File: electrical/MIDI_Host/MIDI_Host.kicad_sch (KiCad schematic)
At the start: 45 parts, among them CN1 USB-CON-AF-LCP-Offset, J1 MC-107DM, J2 (NF), SW1 ST-0-102-C03-N003-RS, SW2 TC-1109DE-C-G, U11 BL1551B, U12 BL1551B, U14 SESRV05-4, U15 SESRV05-4, U16 BL1551B, U17 74HC165, U4 ESP32-S3-WROOM-1U, U8 BL1551B

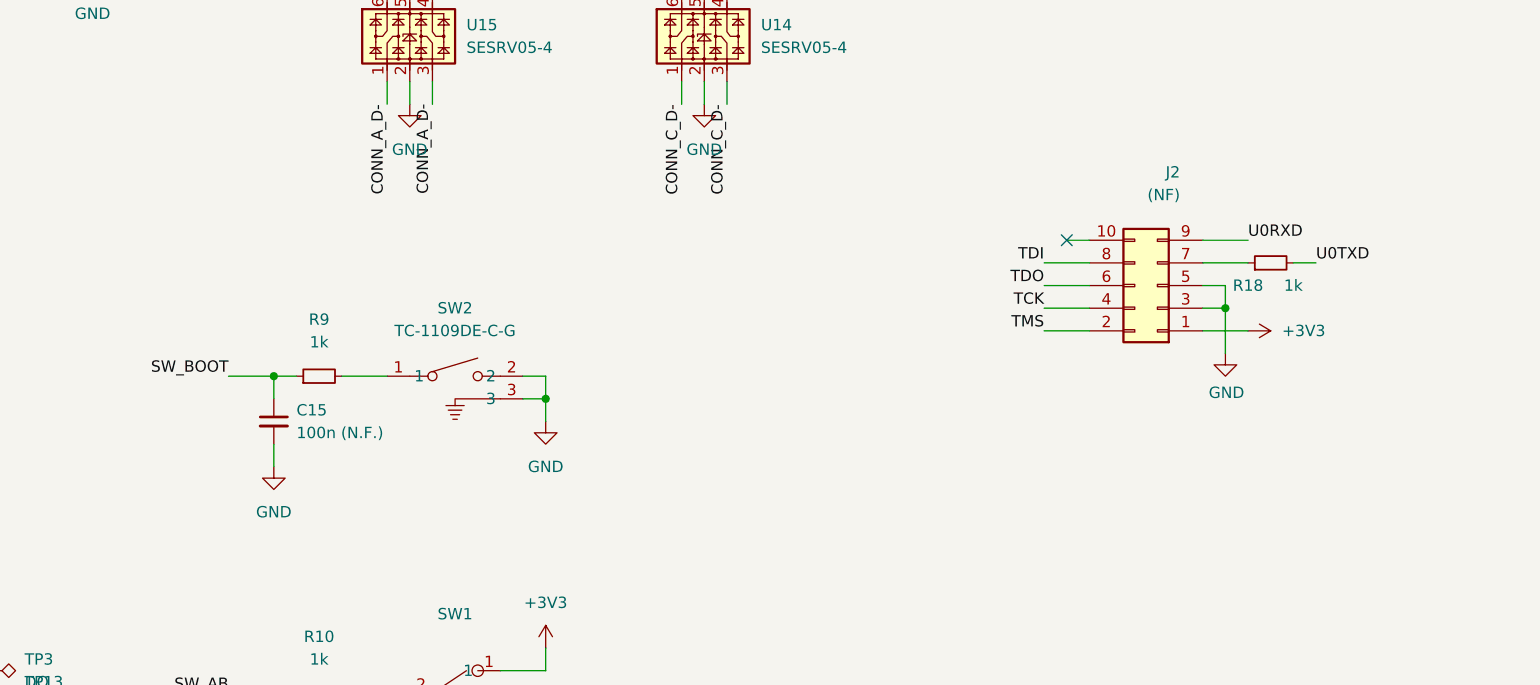
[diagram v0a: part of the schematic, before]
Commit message: SUKU sync + fw connect status led function added
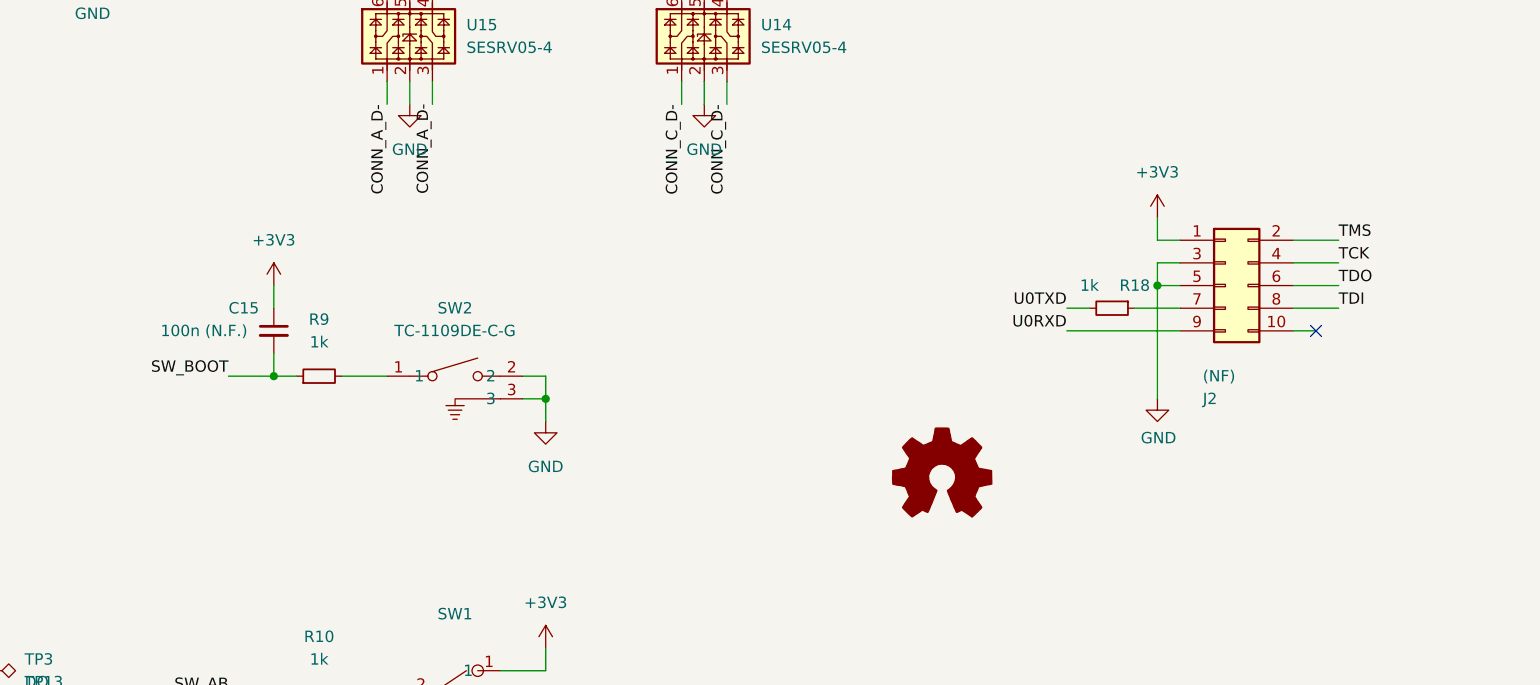
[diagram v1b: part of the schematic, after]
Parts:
- added LOGO1: OSHWA, suku_basics:OSHWA_KNOT, symbol suku_basics:OSHWA
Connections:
- net +3V3: now also C15.1
- net GND: no longer C15.2
- net SW_BOOT: now also C15.2; no longer C15.1
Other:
- moved on the sheet: C15, J2, R18

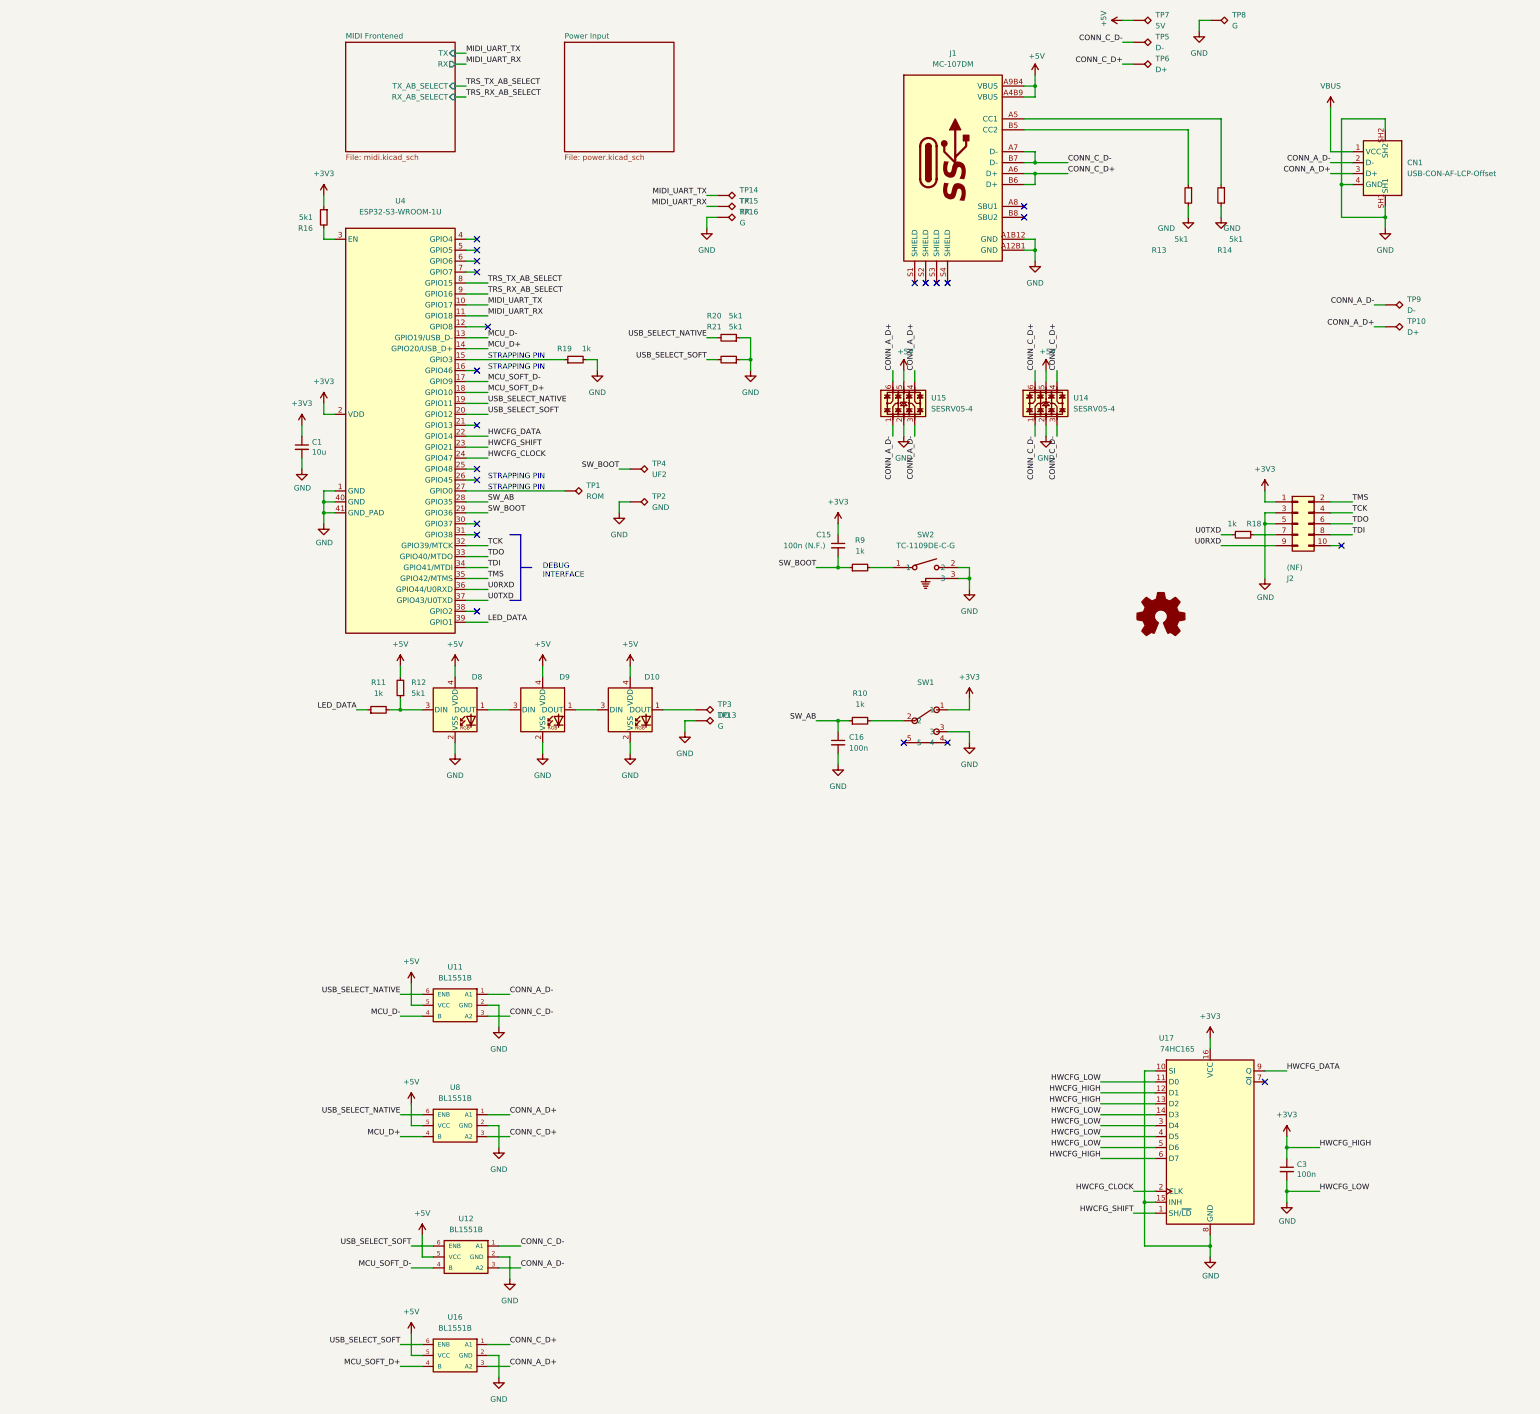
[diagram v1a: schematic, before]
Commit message: SUKU connectors moved back, gerber testpoint names fixed
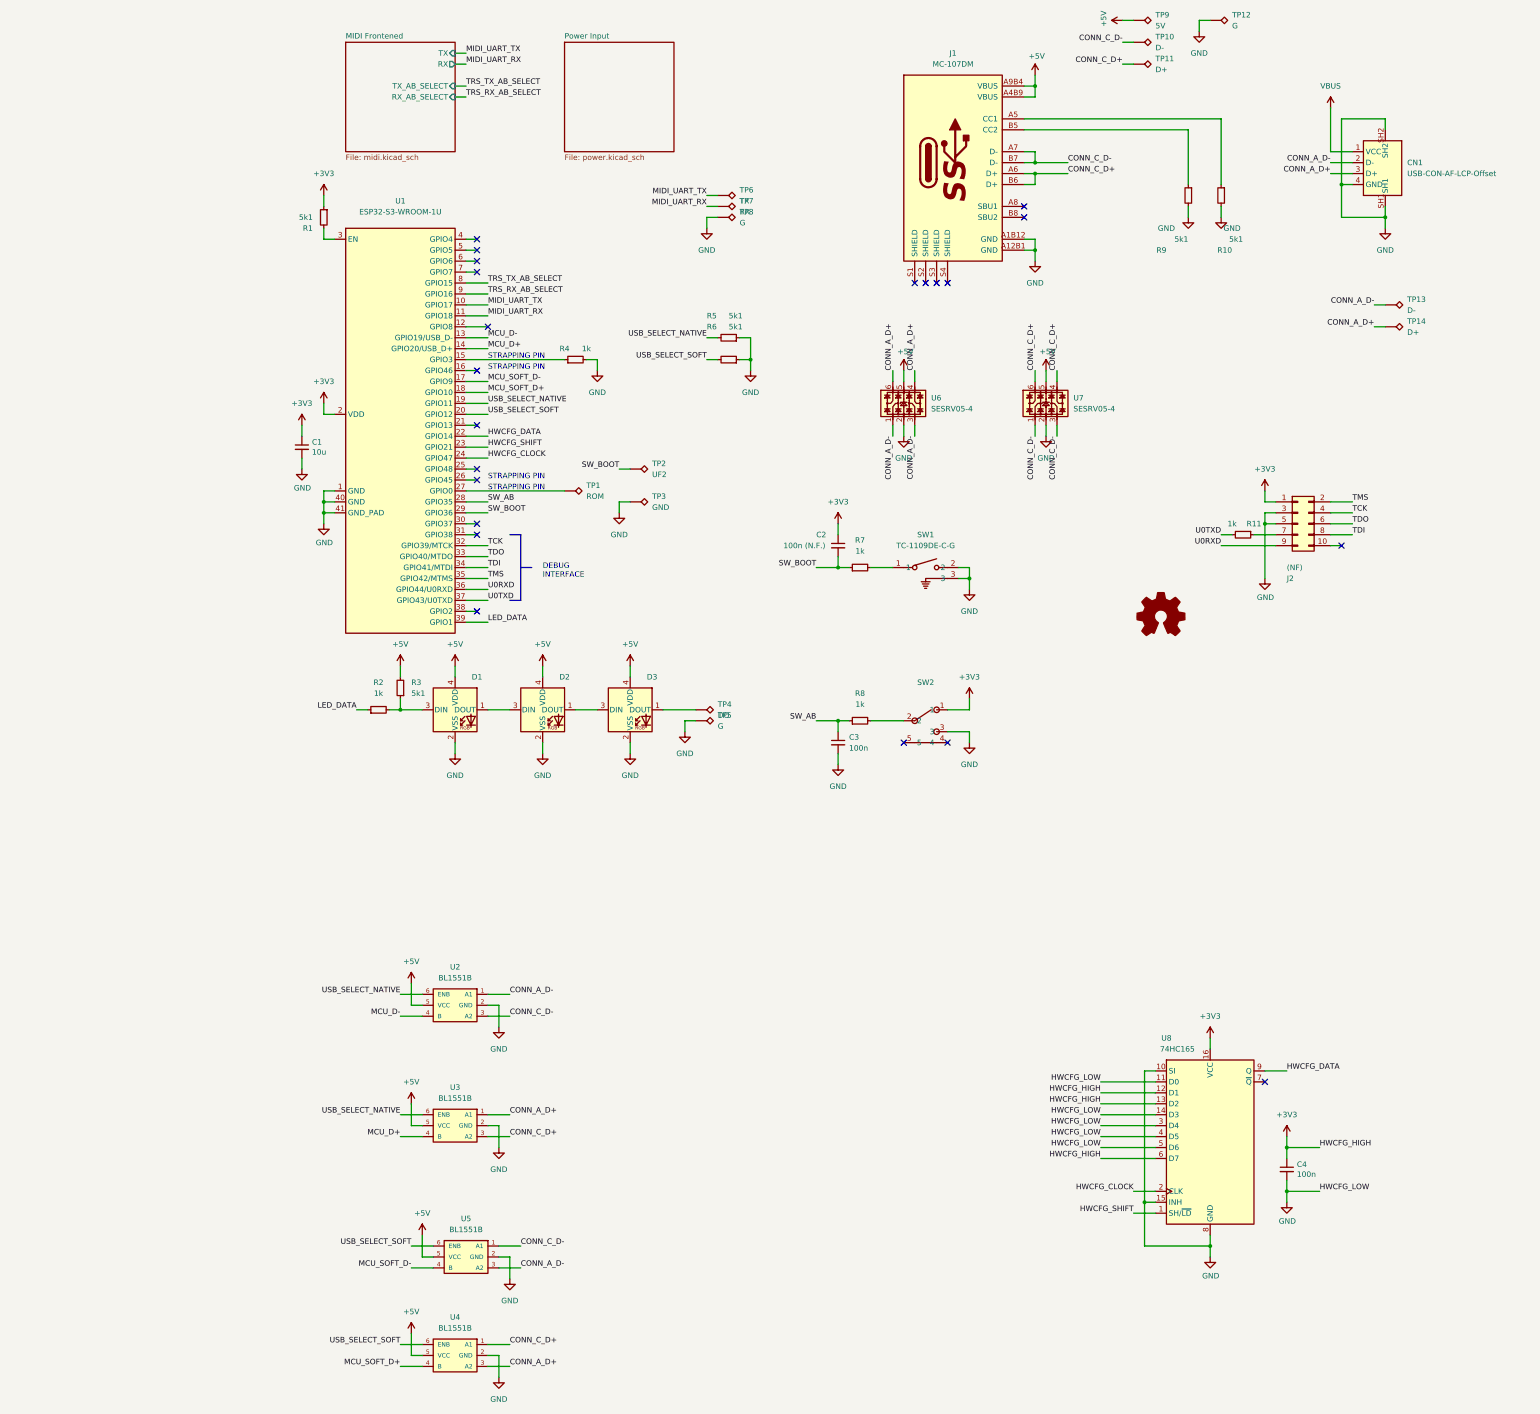
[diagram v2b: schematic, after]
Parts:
- renumbered C15 to C2, C16 to C3, C3 to C4, D8 to D1, D9 to D2, D10 to D3, R16 to R1, R14 to R10, R18 to R11, R11 to R2, R12 to R3, R19 to R4, R20 to R5, R21 to R6, R9 to R7, R10 to R8, R13 to R9, SW2 to SW1, SW1 to SW2, TP5 to TP10, TP6 to TP11, TP8 to TP12, TP9 to TP13, TP10 to TP14, TP4 to TP2, TP2 to TP3, TP3 to TP4, TP13 to TP5, TP14 to TP6, TP15 to TP7, TP16 to TP8, TP7 to TP9, U4 to U1, U11 to U2, U8 to U3, U16 to U4, U12 to U5, U15 to U6, U14 to U7, U17 to U8

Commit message: SUKU v3 laout finished, decoupling and esd protection improved
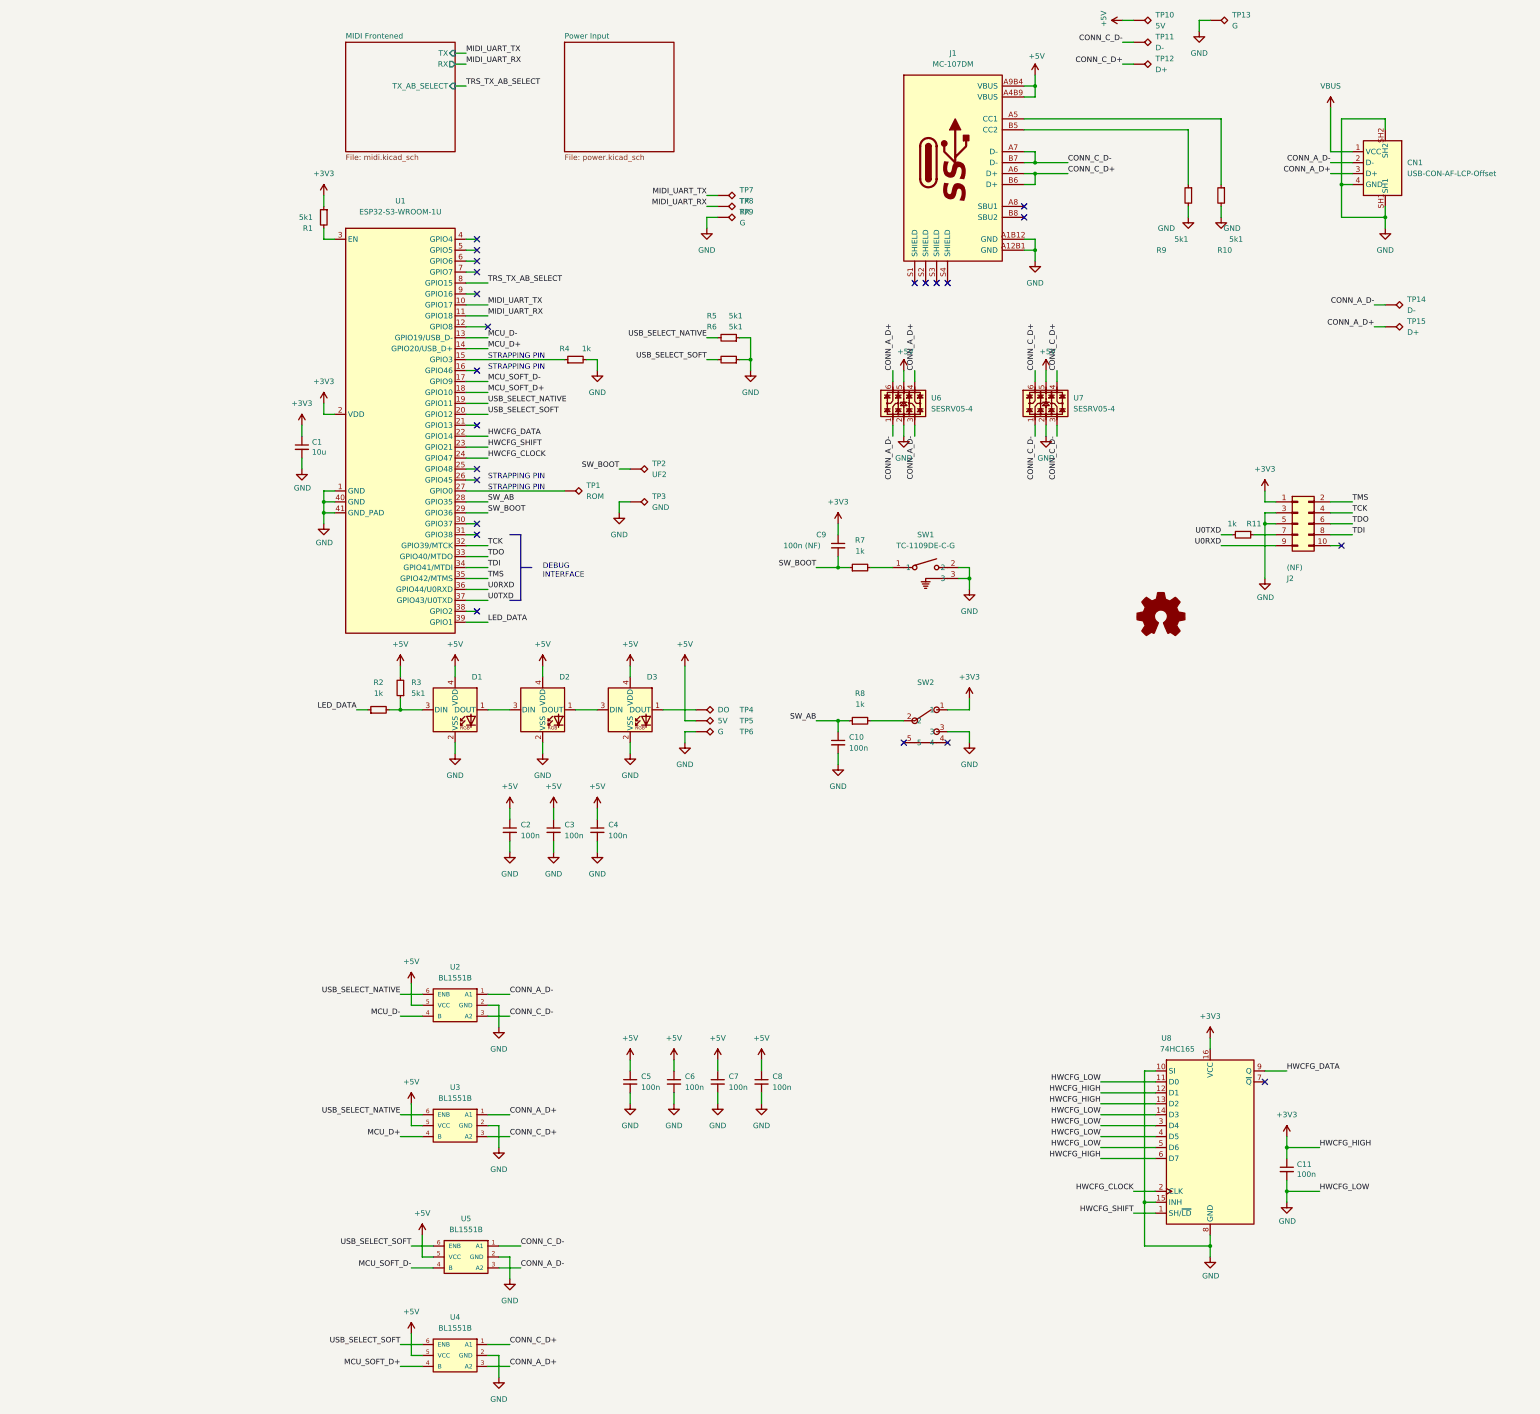
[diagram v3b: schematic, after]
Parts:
- added C2, C3, C4, C5, C6, C7, C8: 100n, suku_basics:CAP_0402, symbol suku_basics:CAP
- added TP5: 5V, TestPoint:TestPoint_THTPad_D1.0mm_Drill0.5mm, symbol Connector:TestPoint_Alt
- C1: footprint suku_basics:CAP_0805 -> suku_basics:CAP_0402
- C10: renamed from C3; footprint suku_basics:CAP_0805 -> suku_basics:CAP_0402
- C11: renamed from C4; footprint suku_basics:CAP_0805 -> suku_basics:CAP_0402
- C9: renamed from C2; value 100n (N.F.) -> 100n (NF); footprint suku_basics:CAP_0805 -> suku_basics:CAP_0402
- R1, R10, R11, R2, R3, R4, R5, R6, R7, R8, R9: footprint suku_basics:RES_0805 -> suku_basics:RES_0402
- renumbered TP9 to TP10, TP10 to TP11, TP11 to TP12, TP12 to TP13, TP13 to TP14, TP14 to TP15, TP5 to TP6, TP6 to TP7, TP7 to TP8, TP8 to TP9
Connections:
- net +5V: now also C2.1, C3.1, C4.1, C5.1, C6.1, C7.1, C8.1, TP5.1
- net GND: now also C2.2, C3.2, C4.2, C5.2, C6.2, C7.2, C8.2
- net TRS_RX_AB_SELECT: no longer names the net of U1.9 (GPIO16)
- no-connect marks 22 -> 23
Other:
- sheet MIDI Frontened ports: added none; removed RX_AB_SELECT
- moved on the sheet: TP6
